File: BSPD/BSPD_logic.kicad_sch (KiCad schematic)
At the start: 6 parts, among them U1 2x4 OR GATE, U2 4081, U3 2x4 OR GATE

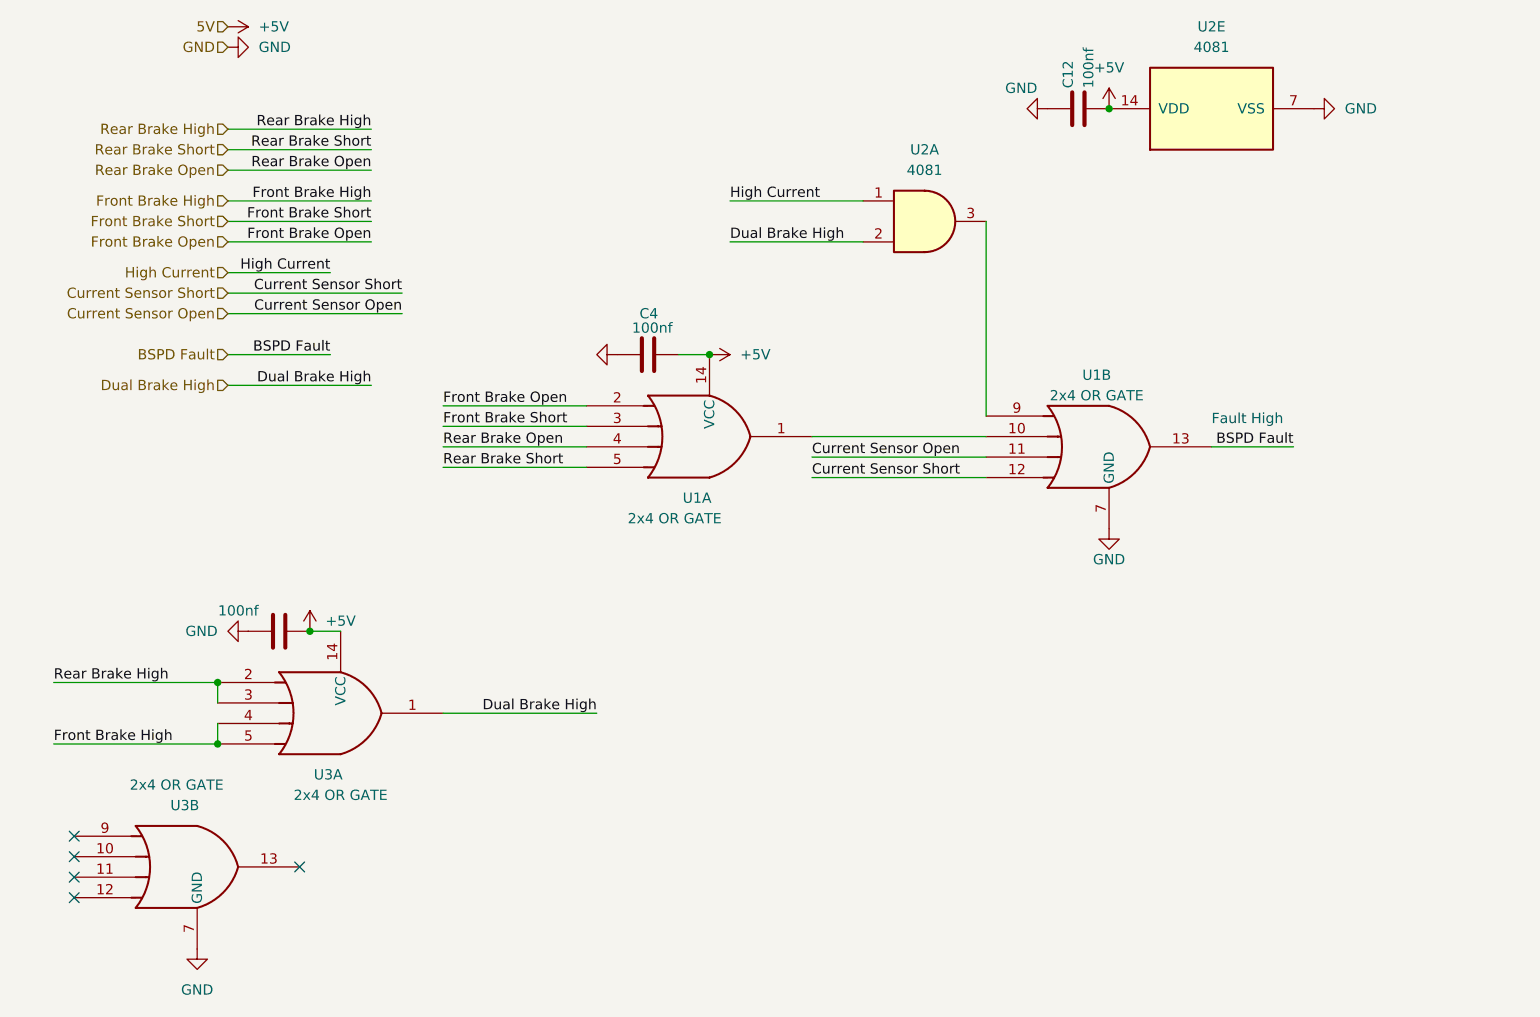
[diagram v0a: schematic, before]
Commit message: Overhaul of BPSD to V3.0
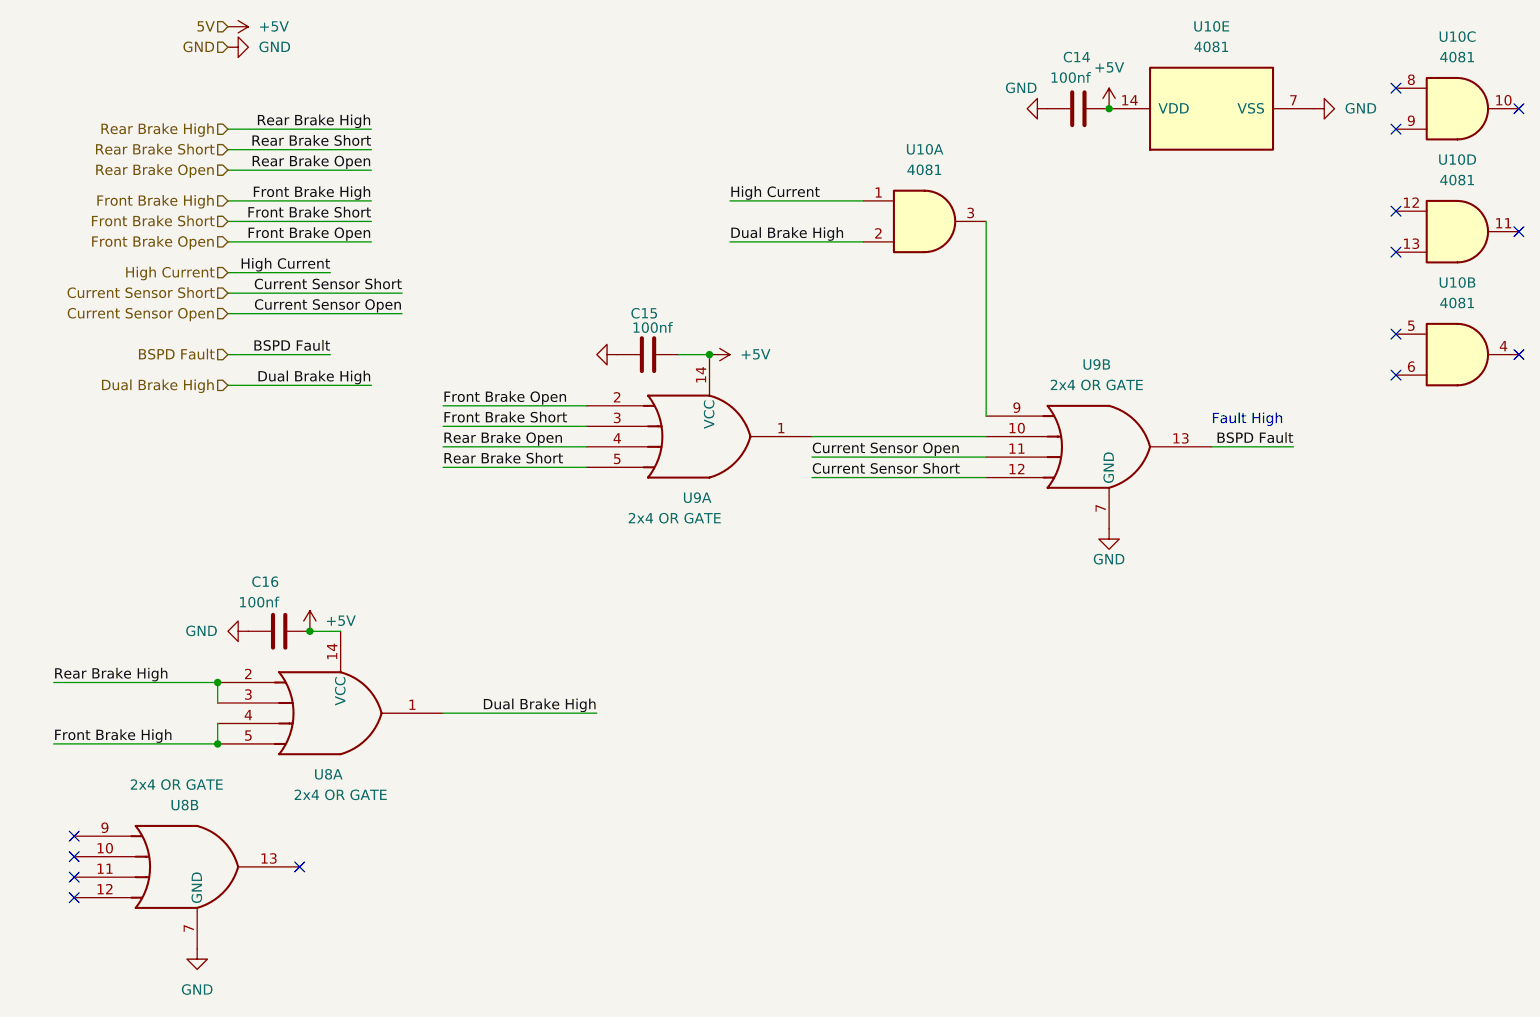
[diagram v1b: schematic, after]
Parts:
- removed U2: 4081, Package_SO:SOIC-14_3.9x8.7mm_P1.27mm, symbol 4xxx:4081
- added U10: 4081, Package_SO:SOIC-14_3.9x8.7mm_P1.27mm, symbol 4xxx:4081
- renumbered C12 to C14, C4 to C15, C7 to C16, U3 to U8, U1 to U9
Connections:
- net +5V: now also U10.14 (VDD)
- net Dual Brake High: now also U10.2
- net GND: now also U10.7 (VSS)
- net High Current: now also U10.1
- net at U9.9: now also U10.3
- no-connect marks 5 -> 14
